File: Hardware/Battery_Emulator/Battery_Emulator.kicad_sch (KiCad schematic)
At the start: 8 parts, among them J1 Screw_Terminal_01x02, J2 USB4105-GF-A-060, U10 ATmega328PB-A, U3 74AHC2G125DP,125, U4 FT230XS-R, U5 LM7805_TO220, U9 ECS-160-7-33B2-CTN-TR3

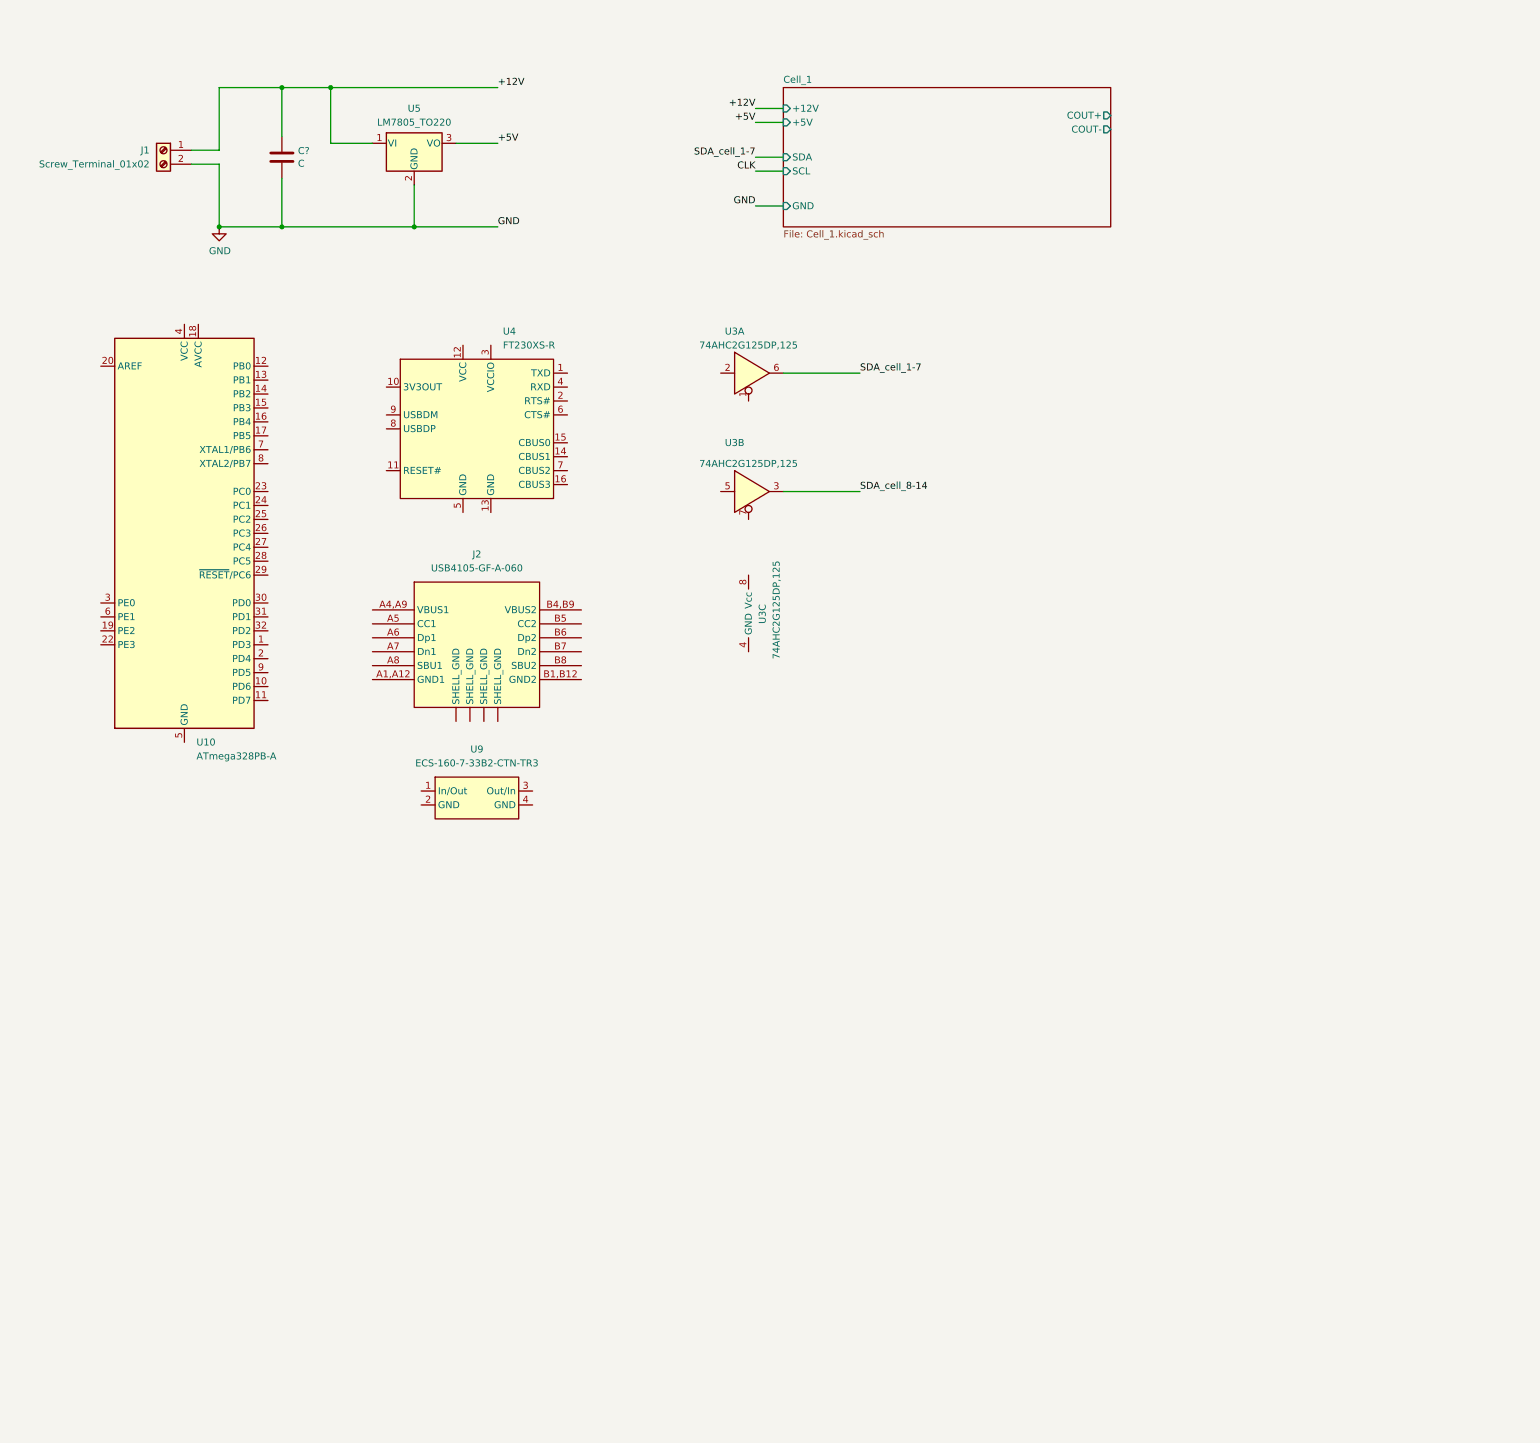
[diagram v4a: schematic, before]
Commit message: Inputted all components and values
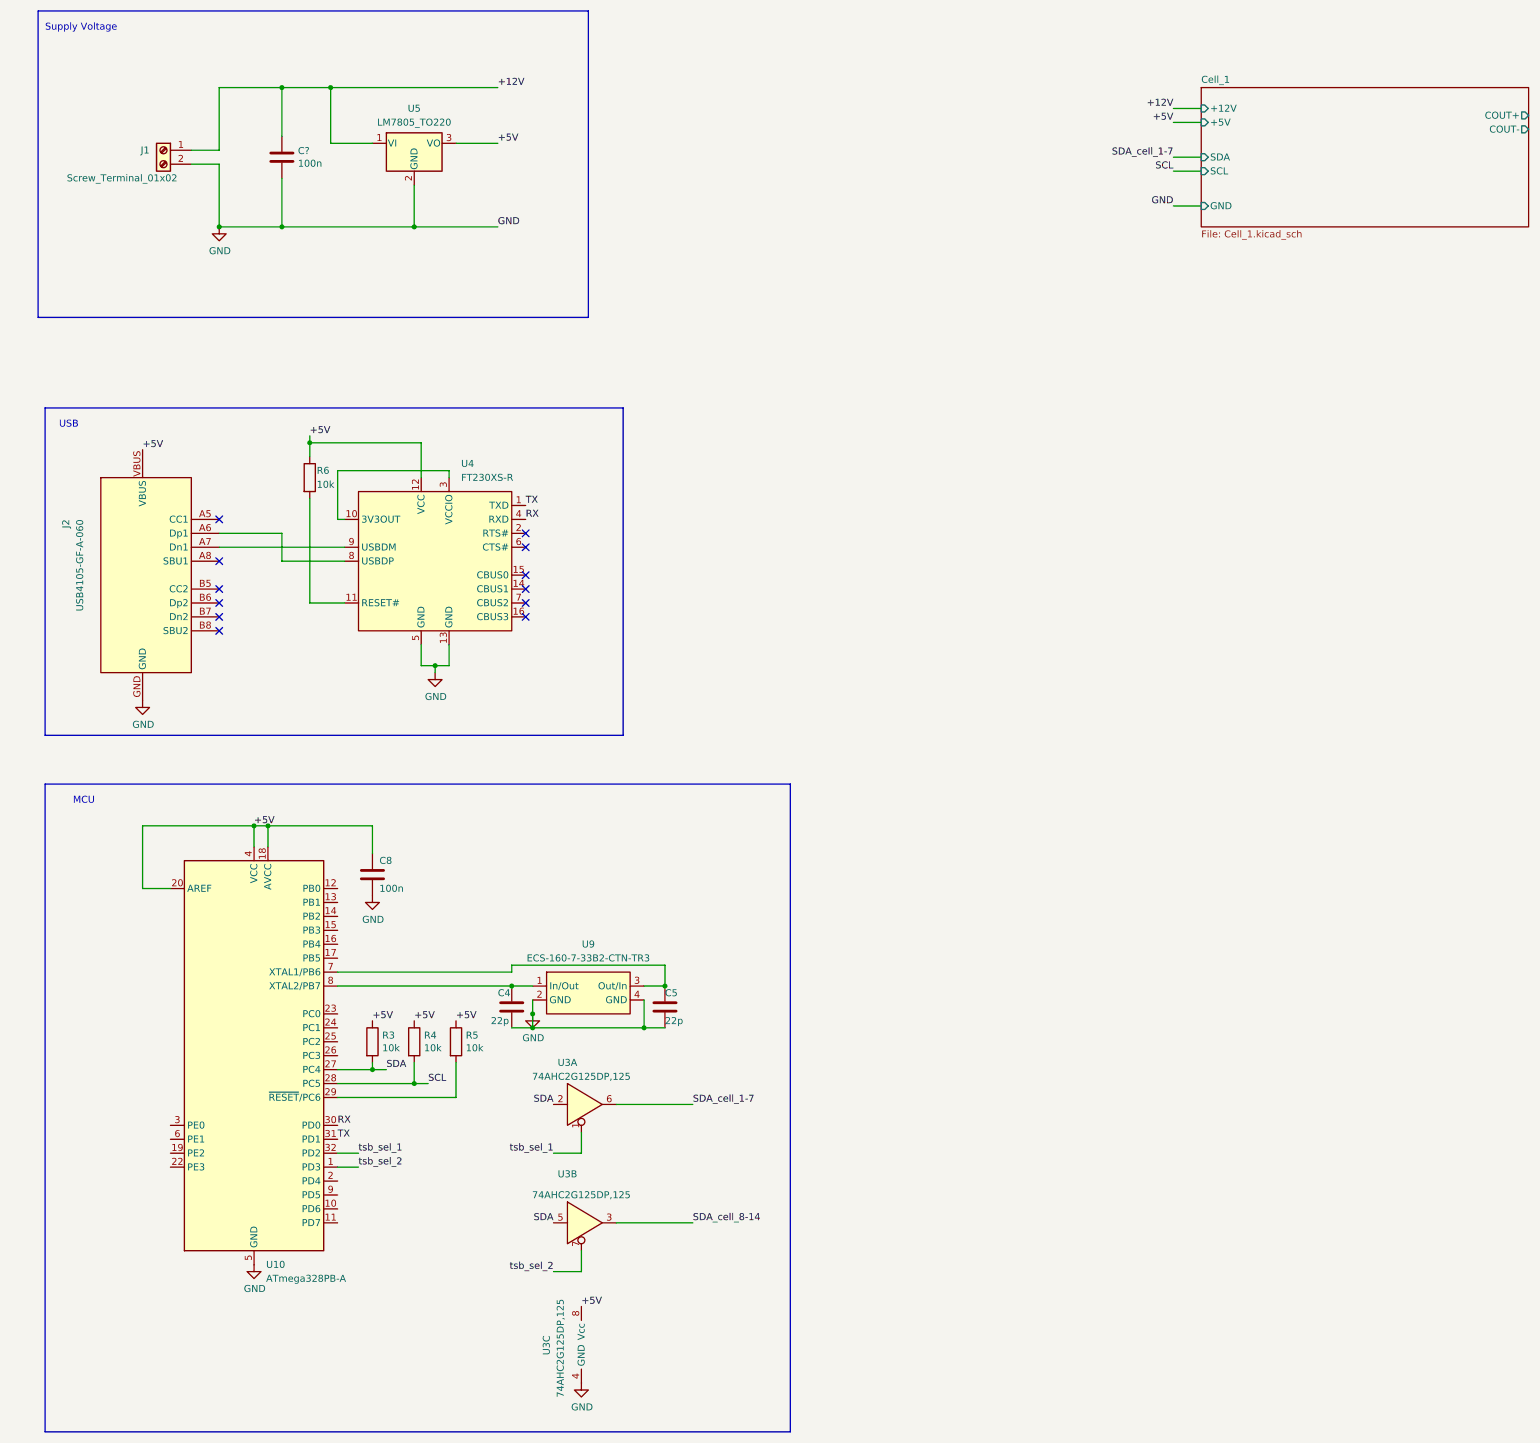
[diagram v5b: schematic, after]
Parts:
- added C4, C5: 22p, Capacitor_SMD:C_0805_2012Metric, symbol Device:C
- added C8: 100n, Capacitor_SMD:C_0805_2012Metric, symbol Device:C
- added R3, R4, R5, R6: 10k, Resistor_SMD:R_0805_2012Metric, symbol Device:R
- C?: value C -> 100n
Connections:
- net +5V: now also J2.VBUS, U10.18 (AVCC), U10.20 (AREF), U10.4 (VCC), U3.8 (Vcc), U4.12 (VCC), C8.1, R3.1, R4.1, R5.1, R6.1
- net GND: now also J2.GND, U10.21 (GND), U10.5 (GND), U3.4 (GND), U4.13 (GND), U4.5 (GND), U9.2 (GND), U9.4 (GND), C4.2, C5.2, C8.2
- net tsb_sel_1: now reaches U3.1
- net tsb_sel_1: now also U10.32 (PD2)
- net SDA: now reaches U3.2
- net SDA: now also U10.27 (PC4), U3.5, R3.2
- net tsb_sel_2: now reaches U10.1 (PD3)
- net tsb_sel_2: now also U3.7
- net SCL: now reaches U10.28 (PC5)
- net SCL: now also R4.2
- net at U10.29 (~{RESET}/PC6): now also R5.2
- net RX: now reaches U10.30 (PD0)
- net RX: now also U4.4 (RXD)
- net TX: now reaches U10.31 (PD1)
- net TX: now also U4.1 (TXD)
- net at U10.7 (XTAL1/PB6): now also U9.3 (Out/In), C5.1
- net at U10.8 (XTAL2/PB7): now also U9.1 (In/Out), C4.1
- net at J2.A6 (Dp1): now also U4.8 (USBDP)
- net at J2.A7 (Dn1): now also U4.9 (USBDM)
- net at U4.10 (3V3OUT): now also U4.3 (VCCIO)
- net at U4.11 (RESET#): now also R6.2
- no-connect marks 0 -> 12
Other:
- note added: "MCU"
- note added: "Supply Voltage"
- note added: "USB"
- moved on the sheet: U10, U3A, U3B, U3C, U4, U9
